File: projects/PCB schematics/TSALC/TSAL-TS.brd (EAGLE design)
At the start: 99.1 x 99.1 mm, 29 parts, among them J1 2P_1-770166-0, J2 2P_1-770166-0, J3 2P_1-770166-0, J4 2P_1-770166-0, X1 5566-2, X2 5566-2

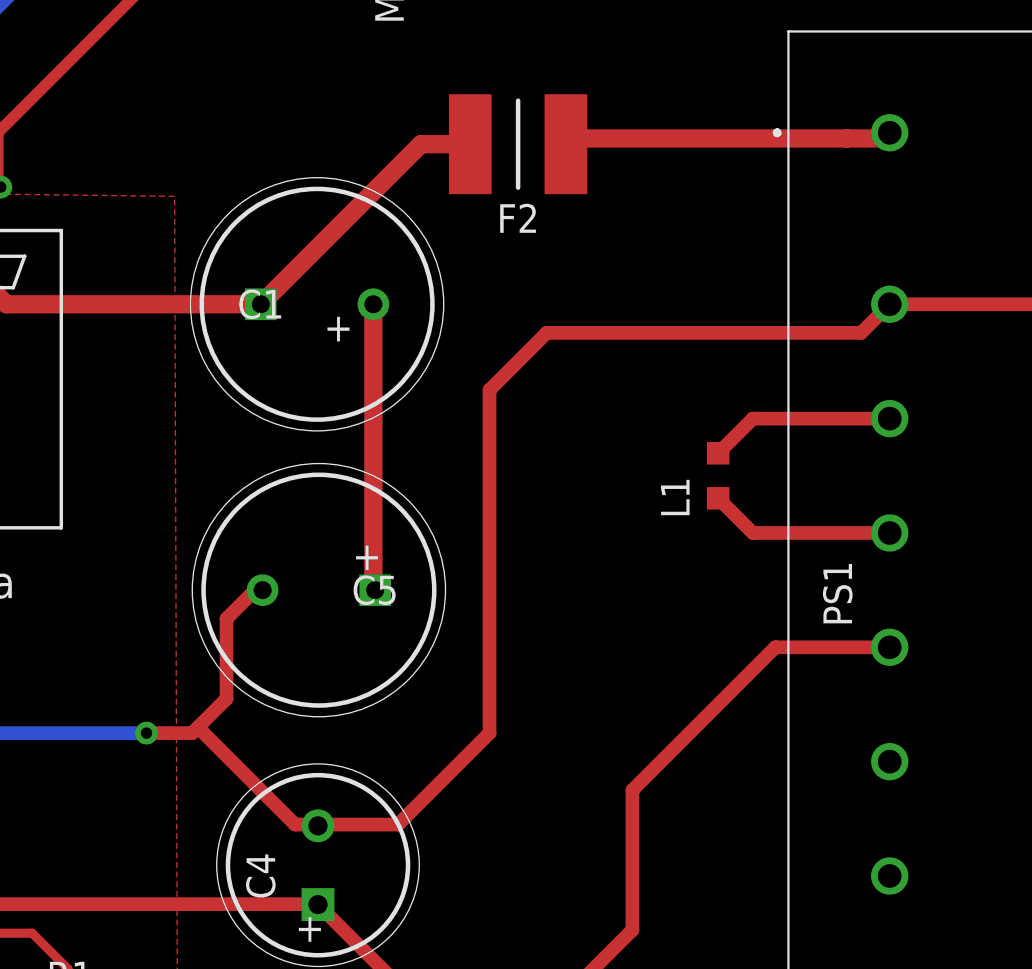
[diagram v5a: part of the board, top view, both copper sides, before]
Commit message: TSAL - Added in fuses.
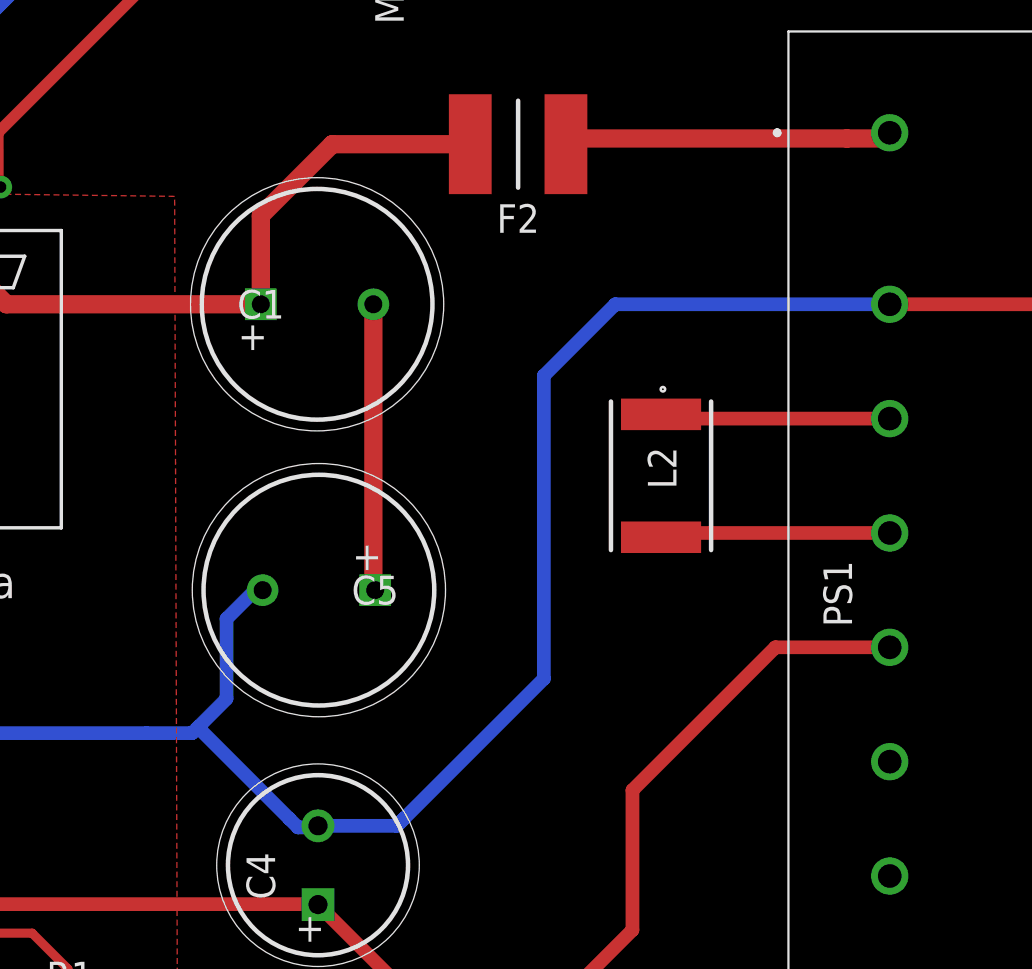
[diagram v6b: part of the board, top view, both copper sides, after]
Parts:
- removed L1: 1mH, rcl:L2012C
- added L2: SDE6603-102M, SDE6603-102M:SDE6603
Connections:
- net N$1: now also L2.2; no longer L1.2
- net N$2: now also L2.1; no longer L1.1
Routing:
- net HV+: track 58.3 -> 60.6 mm
- net N$2: track 8.26 -> 10.2 mm
- net N$1: track 8.26 -> 10.2 mm
- net HV-: track 211.0 -> 210.4 mm, vias 4 -> 3
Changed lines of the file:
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@@
 <text x="58.42" y="77.216" size="1.27" layer="25" rot="R90">MOTORCONTROLLER-</text>
 <text x="56.134" y="52.959" size="1.27" layer="25">+</text>
-<text x="54.864" y="63.119" size="1.27" layer="25">+</text>
+<text x="51.054" y="62.738" size="1.27" layer="25">+</text>
 <text x="53.594" y="36.449" size="1.27" layer="25">+</text>
 <text x="64.9986" y="18.5166" size="1.016" layer="25" font="vector">Authors: github.com/michaelpass
@@
 <attribute name="VALUE" x="82.78" y="51.91" size="1.27" layer="27" rot="R270" align="center"/>
 </element>
-<element name="L1" library="rcl" library_urn="urn:adsk.eagle:library:334" package="L2012C" package3d_urn="urn:adsk.eagle:package:23475/2" value="1mH" x="72.39" y="57.15" smashed="yes" rot="R270">
-<attribute name="NAME" x="71.12" y="55.245" size="1.27" layer="25" rot="R90"/>
-<attribute name="SPICEPREFIX" value="L" x="72.39" y="57.15" size="1.778" layer="27" rot="R270" display="off"/>
-</element>
 <element name="C4" library="EEU-FS1H221L" package="CAPPRD350W65D800H2200" value="EEU-FS1H221L" x="54.61" y="38.1" smashed="yes" rot="R90">
 <attribute name="DESCRIPTION" value="Aluminum Electrolytic Capacitors - Radial Leaded 50VDC 220uF 9000H 8x20mm" x="54.61" y="38.1" size="1.778" layer="27" rot="R90" display="off"/>
@@
 <attribute name="NAME" x="63.5" y="68.58" size="1.27" layer="25" align="center"/>
 <attribute name="VALUE" x="63.5" y="71.882" size="1.27" layer="27" align="center"/>
+</element>
+<element name="L2" library="SDE6603-102M" package="SDE6603" value="SDE6603-102M" x="69.85" y="57.15" smashed="yes" rot="R270">
+<attribute name="DESCRIPTION" value="SMD Power Inductor 1000uH 20% 250mA 6603 Bourns SDE6603 Series Shielded Wire-wound SMD Inductor with a Ferrite Core, 1000 uH Wire-Wound 70mA Idc" x="69.85" y="57.15" size="1.778" layer="27" rot="R270" display="off"/>
+<attribute name="HEIGHT" value="mm" x="69.85" y="57.15" size="1.778" layer="27" rot="R270" display="off"/>
+<attribute name="MANUFACTURER_NAME" value="Bourns" x="69.85" y="57.15" size="1.778" layer="27" rot="R270" display="off"/>
+<attribute name="MANUFACTURER_PART_NUMBER" value="SDE6603-102M" x="69.85" y="57.15" size="1.778" layer="27" rot="R270" display="off"/>
+<attribute name="MOUSER_PART_NUMBER" value="652-SDE6603-102M" x="69.85" y="57.15" size="1.778" layer="27" rot="R270" display="off"/>
+<attribute name="MOUSER_PRICE-STOCK" value="https://www.mouser.com/Search/Refine.aspx?Keyword=652-SDE6603-102M" x="69.85" y="57.15" size="1.778" layer="27" rot="R270" display="off"/>
+<attribute name="NAME" x="69.90163125" y="57.49565" size="1.27" layer="25" rot="R270" align="center"/>
+<attribute name="VALUE" x="69.90163125" y="57.49565" size="1.27" layer="27" rot="R270" align="center"/>
 </element>
 </elements>
@@
 <wire x1="91.44" y1="68.58" x2="87.63" y2="64.77" width="0.6096" layer="1"/>
 <wire x1="87.63" y1="64.77" x2="80.01" y2="64.77" width="0.6096" layer="1"/>
-<wire x1="62.23" y1="45.72" x2="62.23" y2="60.96" width="0.6096" layer="1"/>
-<wire x1="62.23" y1="45.72" x2="58.166" y2="41.656" width="0.6096" layer="1"/>
-<wire x1="58.166" y1="41.656" x2="54.61" y2="41.656" width="0.6096" layer="1"/>
-<wire x1="54.61" y1="41.656" x2="54.61" y2="41.6" width="0.6096" layer="1"/>
+<wire x1="64.643" y1="48.133" x2="64.643" y2="61.595" width="0.6096" layer="16"/>
+<wire x1="64.643" y1="48.133" x2="58.42" y2="41.91" width="0.6096" layer="16"/>
+<wire x1="58.42" y1="41.91" x2="58.166" y2="41.656" width="0.6096" layer="16"/>
 <wire x1="18.0315" y1="33.782" x2="18.0315" y2="37.4015" width="0.6096" layer="1"/>
 <wire x1="18.0315" y1="37.4015" x2="18.095" y2="37.465" width="0.6096" layer="1"/>
@@
 <wire x1="21.59" y1="39.37" x2="18.476" y2="39.37" width="0.6096" layer="1"/>
 <wire x1="23.21625" y1="40.99625" x2="21.59" y2="39.37" width="0.6096" layer="1"/>
-<wire x1="62.23" y1="60.96" x2="64.77" y2="63.5" width="0.6096" layer="1"/>
-<wire x1="78.74" y1="63.5" x2="64.77" y2="63.5" width="0.6096" layer="1"/>
-<wire x1="78.74" y1="63.5" x2="80.01" y2="64.77" width="0.6096" layer="1"/>
 <wire x1="91.44" y1="74.93" x2="91.44" y2="68.58" width="0.6096" layer="1"/>
 <wire x1="75.7682" y1="86.0298" x2="76.2" y2="86.0298" width="0.6096" layer="1"/>
@@
 <via x="34.29" y="45.72" extent="1-16" drill="0.508"/>
 <wire x1="34.29" y1="45.72" x2="46.99" y2="45.72" width="0.6096" layer="16"/>
-<via x="46.99" y="45.72" extent="1-16" drill="0.508"/>
-<wire x1="46.99" y1="45.72" x2="49.022" y2="45.72" width="0.6096" layer="1"/>
-<wire x1="49.022" y1="45.72" x2="49.276" y2="45.974" width="0.6096" layer="1"/>
-<wire x1="49.276" y1="45.974" x2="50.546" y2="47.244" width="0.6096" layer="1"/>
-<wire x1="50.546" y1="47.244" x2="50.546" y2="50.8" width="0.6096" layer="1"/>
-<wire x1="51.816" y1="52.07" x2="50.546" y2="50.8" width="0.6096" layer="1"/>
+<wire x1="46.99" y1="45.72" x2="49.022" y2="45.72" width="0.6096" layer="16"/>
+<wire x1="49.022" y1="45.72" x2="49.276" y2="45.974" width="0.6096" layer="16"/>
+<wire x1="49.276" y1="45.974" x2="50.546" y2="47.244" width="0.6096" layer="16"/>
+<wire x1="50.546" y1="47.244" x2="50.546" y2="50.8" width="0.6096" layer="16"/>
 <wire x1="18.415" y1="47.05" x2="18.415" y2="41.85" width="0.4064" layer="1"/>
 <wire x1="17.145" y1="47.05" x2="17.145" y2="41.85" width="0.4064" layer="1"/>
 <contactref element="C5" pad="2"/>
-<wire x1="49.276" y1="45.974" x2="53.594" y2="41.656" width="0.6096" layer="1"/>
-<wire x1="53.594" y1="41.656" x2="54.61" y2="41.656" width="0.6096" layer="1"/>
-<wire x1="52.15" y1="52.07" x2="51.816" y2="52.07" width="0.6096" layer="1"/>
+<wire x1="49.276" y1="45.974" x2="53.34" y2="41.91" width="0.6096" layer="16"/>
+<wire x1="53.721" y1="41.529" x2="53.34" y2="41.91" width="0.6096" layer="16"/>
 <wire x1="76.2" y1="90.17" x2="76.2" y2="95.377" width="1.27" layer="1"/>
 <wire x1="76.2" y1="95.377" x2="75.057" y2="96.52" width="1.27" layer="1"/>
 <wire x1="75.057" y1="96.52" x2="69.784" y2="96.52" width="1.27" layer="1"/>
+<wire x1="64.643" y1="61.595" x2="67.818" y2="64.77" width="0.6096" layer="16"/>
+<wire x1="67.818" y1="64.77" x2="80.01" y2="64.77" width="0.6096" layer="16"/>
+<wire x1="58.42" y1="41.91" x2="58.11" y2="41.6" width="0.6096" layer="16"/>
+<wire x1="58.11" y1="41.6" x2="54.61" y2="41.6" width="0.6096" layer="16"/>
+<wire x1="54.61" y1="41.6" x2="54.539" y2="41.529" width="0.6096" layer="16"/>
+<wire x1="54.539" y1="41.529" x2="53.721" y2="41.529" width="0.6096" layer="16"/>
+<wire x1="50.546" y1="50.8" x2="51.816" y2="52.07" width="0.6096" layer="16"/>
+<wire x1="51.816" y1="52.07" x2="52.15" y2="52.07" width="0.6096" layer="16"/>
 </signal>
 <signal name="VCC">
@@
 <wire x1="30.48" y1="75.057" x2="40.767" y2="64.77" width="0.8128" layer="1"/>
 <contactref element="F2" pad="1"/>
-<wire x1="59.182" y1="71.882" x2="61.375" y2="71.882" width="0.8128" layer="1"/>
-<wire x1="52.07" y1="64.77" x2="59.182" y2="71.882" width="0.8128" layer="1"/>
+<wire x1="55.245" y1="71.882" x2="61.375" y2="71.882" width="0.8128" layer="1"/>
+<wire x1="52.07" y1="64.77" x2="52.07" y2="68.707" width="0.8128" layer="1"/>
+<wire x1="55.245" y1="71.882" x2="52.07" y2="68.707" width="0.8128" layer="1"/>
 </signal>
 <signal name="N$1">
-<contactref element="L1" pad="2"/>
 <contactref element="PS1" pad="8"/>
-<wire x1="80.01" y1="54.61" x2="73.93" y2="54.61" width="0.6096" layer="1"/>
-<wire x1="72.39" y1="56.15" x2="73.93" y2="54.61" width="0.6096" layer="1"/>
+<contactref element="L2" pad="2"/>
+<wire x1="70.04" y1="54.61" x2="69.85" y2="54.42" width="0.6096" layer="1"/>
+<wire x1="80.01" y1="54.61" x2="70.04" y2="54.61" width="0.6096" layer="1"/>
 </signal>
 <signal name="N$2">
 <contactref element="PS1" pad="6"/>
-<contactref element="L1" pad="1"/>
-<wire x1="73.93" y1="59.69" x2="72.39" y2="58.15" width="0.6096" layer="1"/>
-<wire x1="73.93" y1="59.69" x2="80.01" y2="59.69" width="0.6096" layer="1"/>
+<contactref element="L2" pad="1"/>
+<wire x1="70.04" y1="59.69" x2="69.85" y2="59.88" width="0.6096" layer="1"/>
+<wire x1="80.01" y1="59.69" x2="70.04" y2="59.69" width="0.6096" layer="1"/>
 </signal>
 <signal name="+15V-NONISO">

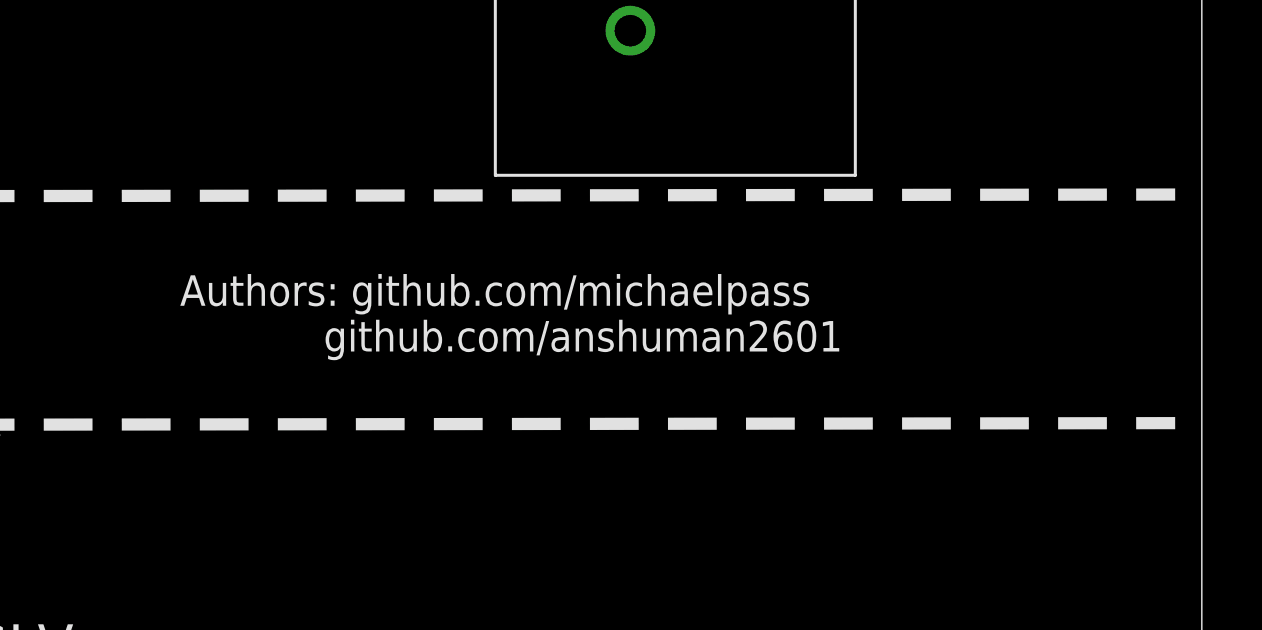
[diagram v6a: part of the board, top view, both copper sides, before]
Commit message: ACCUM - Added IMD fuses.
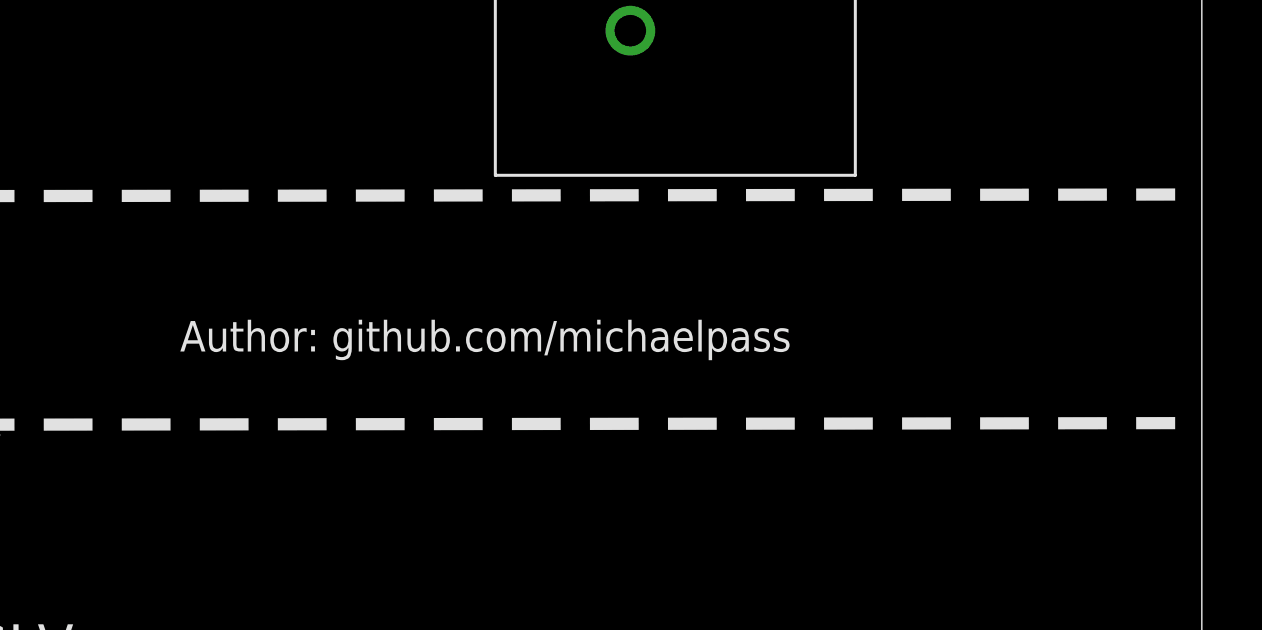
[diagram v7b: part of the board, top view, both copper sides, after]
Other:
- board text added: "Author: github.com/michaelpass"
- board text removed: "Authors: github.com/michaelpass github.com/anshuman2601"
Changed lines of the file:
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@@
 <text x="51.054" y="62.738" size="1.27" layer="25">+</text>
 <text x="53.594" y="36.449" size="1.27" layer="25">+</text>
-<text x="64.9986" y="18.5166" size="1.016" layer="25" font="vector">Authors: github.com/michaelpass
-            github.com/anshuman2601             </text>
+<text x="64.9986" y="18.5166" size="1.016" layer="25" font="vector">Author: github.com/michaelpass</text>
 <text x="57.912" y="8.001" size="1.4224" layer="25" font="vector">GLV:</text>
 <text x="57.658" y="3.81" size="0.9144" layer="25" font="vector">1. TSAL_CONTROL_SIGNAL (OUTPUT) - X1
